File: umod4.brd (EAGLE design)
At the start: 104.9 x 69.8 mm, 101 parts, among them IC1 27C256-FEED-THRU, M1 Generic single-sided NEO-8, M2 RPi Pico W, Q1 DNP/SI2301CDS, Q2 SS8050, U1 RP2040, U2 W25Q128JVSIQ, U3 SY6280AAC, U4 74LVC2G04, U5 74LVC541, U6 74LVC541, U7 74LVC4245, U8 TLV75733P, Y1 12MHz

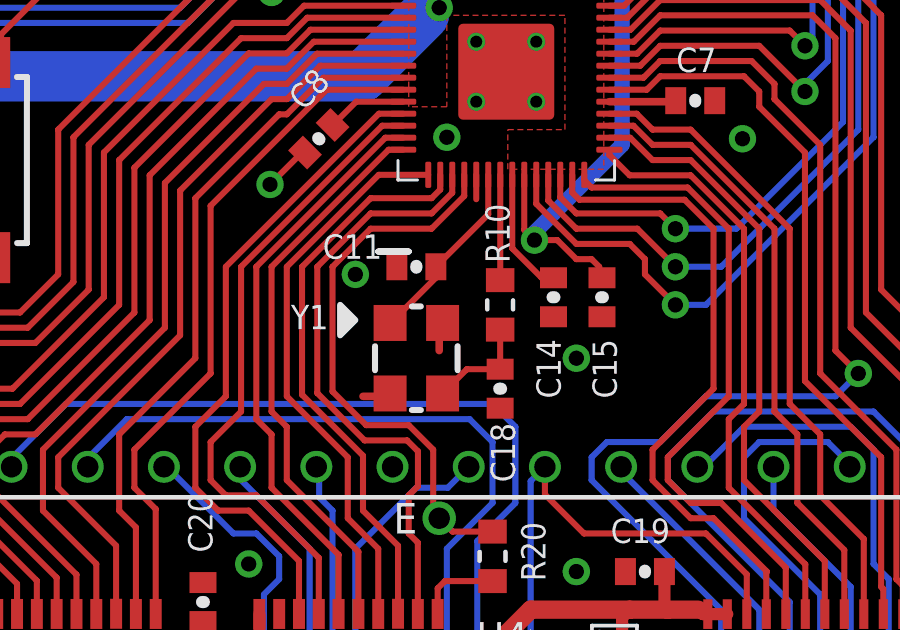
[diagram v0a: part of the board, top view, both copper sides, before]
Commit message: Replace 33pF 0402 packages with SMD-0402-NOM
- Affected parts: C11, C18
- LCSC_PART unchanged
- Manually reworked wire angles on board to clear DRC failures from the new pad geometry
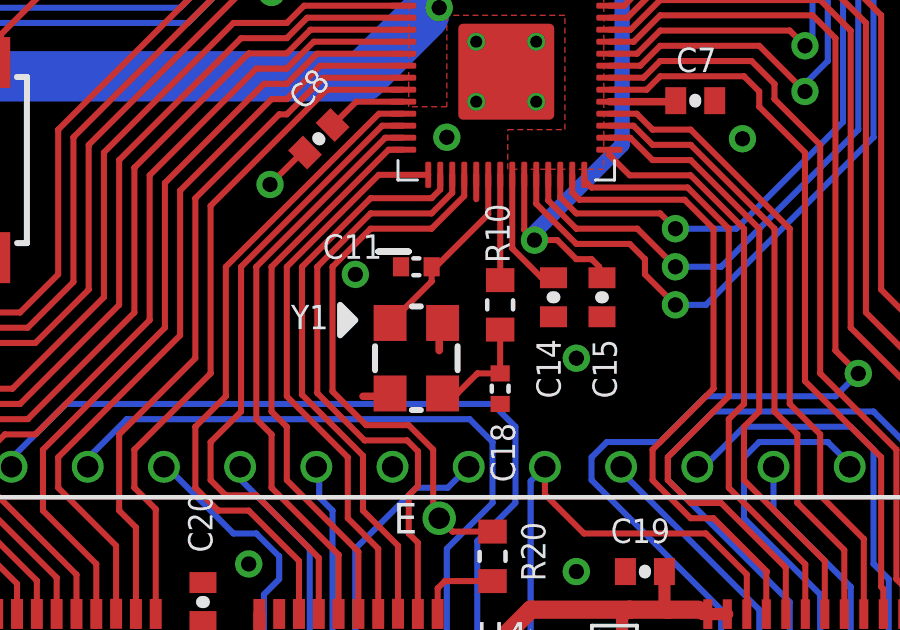
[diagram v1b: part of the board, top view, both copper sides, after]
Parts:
- C11, C18: device SparkFun-03-01-2010:0402-CAP -> robins-v7:SMD-0402-NOM
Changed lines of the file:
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@@
 <attribute name="LCSC_PART" value="C21190" x="87.884" y="35.56" size="1.778" layer="27" rot="R270" display="off"/>
 </element>
-<element name="C11" library="SparkFun-03-01-2010" package="0402-CAP" value="33p/6.3V/COG" x="85.09" y="36.83" smashed="yes">
+<element name="C11" library="robins-v7" package="SMD-0402-NOM" value="33p/6.3V/COG" x="85.09" y="36.83" smashed="yes">
 <attribute name="NAME" x="83.947" y="37.9095" size="0.8128" layer="25" font="vector" ratio="14" rot="R180"/>
 <attribute name="VALUE" x="84.0105" y="35.687" size="0.4064" layer="27"/>
 <attribute name="LCSC_PART" value="C1562" x="85.09" y="36.83" size="1.778" layer="27" display="off"/>
 </element>
-<element name="C18" library="SparkFun-03-01-2010" package="0402-CAP" value="33p/6.3V/COG" x="87.884" y="32.766" smashed="yes" rot="R90">
+<element name="C18" library="robins-v7" package="SMD-0402-NOM" value="33p/6.3V/COG" x="87.884" y="32.766" smashed="yes" rot="R90">
 <attribute name="NAME" x="87.5665" y="31.623" size="0.8128" layer="25" font="vector" ratio="14" rot="R270"/>
 <attribute name="VALUE" x="89.027" y="31.6865" size="0.4064" layer="27" rot="R90"/>
@@
 <contactref element="R10" pad="2"/>
 <contactref element="C18" pad="2"/>
-<wire x1="87.884" y1="33.416" x2="87.884" y2="34.735" width="0.2032" layer="1"/>
-<wire x1="87.884" y1="33.416" x2="86.774" y2="33.416" width="0.2032" layer="1"/>
-<wire x1="86.774" y1="33.416" x2="85.965" y2="32.607" width="0.2032" layer="1"/>
+<wire x1="87.884" y1="33.276" x2="87.884" y2="34.735" width="0.2032" layer="1"/>
+<wire x1="87.884" y1="33.276" x2="87.124" y2="33.276" width="0.2032" layer="1"/>
+<wire x1="85.965" y1="32.607" x2="86.455" y2="32.607" width="0.2032" layer="1"/>
+<wire x1="86.455" y1="32.607" x2="87.124" y2="33.276" width="0.2032" layer="1"/>
 </signal>
 <signal name="N$2">
@@
 <wire x1="87.4872" y1="39.8949" x2="87.4872" y2="38.5772" width="0.2032" layer="1"/>
 <wire x1="84.215" y1="34.957" x2="84.233" y2="34.957" width="0.2032" layer="1"/>
-<wire x1="84.233" y1="34.957" x2="85.74" y2="36.464" width="0.2032" layer="1"/>
-<wire x1="85.74" y1="36.83" x2="85.74" y2="36.464" width="0.2032" layer="1"/>
-<wire x1="87.4872" y1="38.5772" x2="85.74" y2="36.83" width="0.2032" layer="1"/>
+<wire x1="85.6" y1="36.83" x2="85.6" y2="36.342" width="0.2032" layer="1"/>
+<wire x1="85.6" y1="36.342" x2="84.215" y2="34.957" width="0.2032" layer="1"/>
+<wire x1="85.6" y1="36.83" x2="85.74" y2="36.83" width="0.2032" layer="1"/>
+<wire x1="85.74" y1="36.83" x2="87.4872" y2="38.5772" width="0.2032" layer="1"/>
 </signal>
 <signal name="N$5">

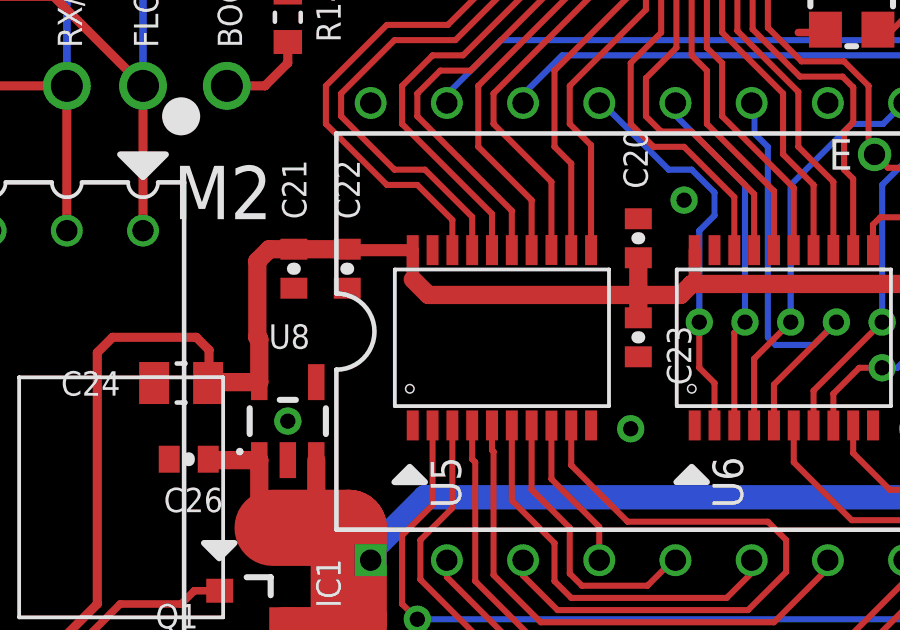
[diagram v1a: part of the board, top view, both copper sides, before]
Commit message: Replace 1uF 0402 packages with SMD-0402-NOM
- Affected parts: C21, C23
- LCSC_PART unchanged
- Manually reworked wire angles on board to clear DRC failures from the new pad geometry
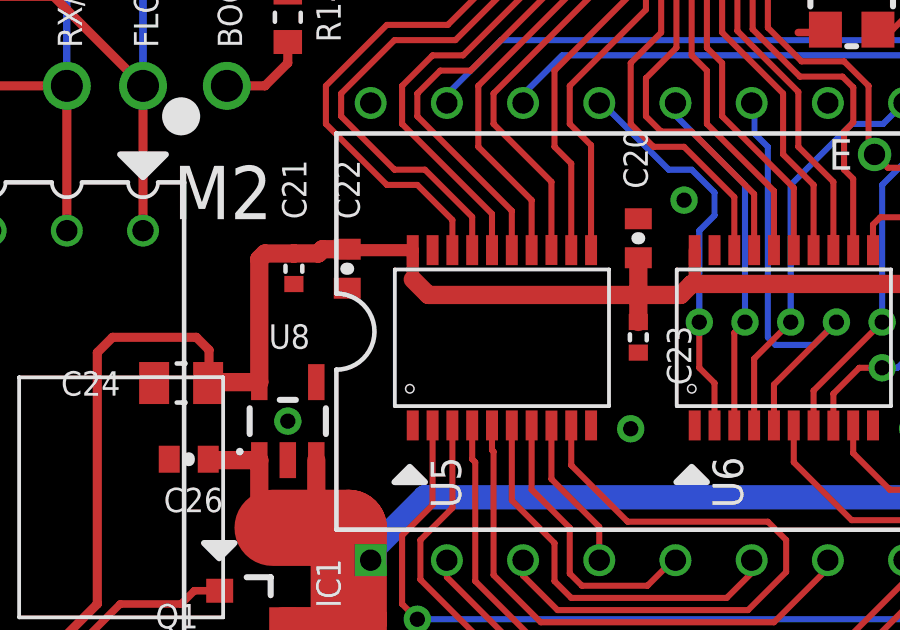
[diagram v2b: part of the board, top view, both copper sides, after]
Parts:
- C21, C23: device SparkFun-03-01-2010:0402-CAP -> robins-v7:SMD-0402-NOM
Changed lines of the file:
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@@
 <attribute name="LCSC_PART" value="C1525" x="77.978" y="25.654" size="1.778" layer="27" rot="R90" display="off"/>
 </element>
-<element name="C23" library="SparkFun-03-01-2010" package="0402-CAP" value="1u/25V/X5R" x="77.978" y="22.352" smashed="yes" rot="R270">
+<element name="C23" library="robins-v7" package="SMD-0402-NOM" value="1u/25V/X5R" x="77.978" y="22.352" smashed="yes" rot="R270">
 <attribute name="NAME" x="78.9305" y="22.733" size="0.8128" layer="25" font="vector" ratio="14" rot="R270"/>
 <attribute name="VALUE" x="76.835" y="23.4315" size="0.4064" layer="27" rot="R270"/>
@@
 <attribute name="LCSC_PART" value="C1525" x="68.2752" y="24.638" size="1.778" layer="27" rot="R270" display="off"/>
 </element>
-<element name="C21" library="SparkFun-03-01-2010" package="0402-CAP" value="1u/25V/X5R" x="66.4972" y="24.638" smashed="yes" rot="R270">
+<element name="C21" library="robins-v7" package="SMD-0402-NOM" value="1u/25V/X5R" x="66.4972" y="24.638" smashed="yes" rot="R270">
 <attribute name="NAME" x="66.9163" y="26.289" size="0.8128" layer="25" font="vector" ratio="14" rot="R90"/>
 <attribute name="VALUE" x="65.3542" y="25.7175" size="0.4064" layer="27" rot="R270"/>
@@
 <wire x1="70.4592" y1="25.257" x2="68.3062" y2="25.257" width="0.4064" layer="1"/>
 <wire x1="68.3062" y1="25.257" x2="68.2752" y2="25.288" width="0.6096" layer="1"/>
-<wire x1="68.2752" y1="25.288" x2="66.4972" y2="25.288" width="0.6096" layer="1"/>
-<wire x1="65.344" y1="20.8581" x2="65.344" y2="22.286" width="0.6096" layer="1"/>
-<wire x1="65.344" y1="22.286" x2="65.278" y2="22.352" width="0.6096" layer="1"/>
-<wire x1="65.278" y1="22.352" x2="65.278" y2="24.892" width="0.6096" layer="1"/>
-<wire x1="65.278" y1="24.892" x2="65.674" y2="25.288" width="0.6096" layer="1"/>
-<wire x1="66.4972" y1="25.288" x2="65.674" y2="25.288" width="0.6096" layer="1"/>
 <wire x1="87.63" y1="24.13" x2="88.9" y2="25.4" width="0.6096" layer="1"/>
 <wire x1="88.9" y1="25.4" x2="92.202" y2="25.4" width="0.6096" layer="1"/>
@@
 <wire x1="77.978" y1="23.764" x2="79.39" y2="23.764" width="0.6096" layer="1"/>
 <wire x1="79.39" y1="23.764" x2="79.756" y2="24.13" width="0.6096" layer="1"/>
-<wire x1="77.978" y1="23.002" x2="77.978" y2="23.764" width="0.6096" layer="1"/>
+<wire x1="77.978" y1="22.862" x2="77.978" y2="23.764" width="0.6096" layer="1"/>
 <wire x1="77.978" y1="25.004" x2="77.978" y2="23.764" width="0.6096" layer="1"/>
 <contactref element="R27" pad="1"/>
@@
 <wire x1="76.962" y1="2.794" x2="76.962" y2="2.286" width="0.3048" layer="1"/>
 <wire x1="76.962" y1="2.286" x2="76.708" y2="2.032" width="0.3048" layer="1"/>
+<wire x1="65.344" y1="20.8581" x2="65.344" y2="24.958" width="0.6096" layer="1"/>
+<wire x1="65.344" y1="24.958" x2="65.532" y2="25.146" width="0.6096" layer="1"/>
+<wire x1="65.532" y1="25.146" x2="66.4952" y2="25.146" width="0.6096" layer="1"/>
+<wire x1="66.4952" y1="25.146" x2="66.4972" y2="25.148" width="0.6096" layer="1"/>
+<wire x1="66.4972" y1="25.148" x2="67.308" y2="25.148" width="0.6096" layer="1"/>
+<wire x1="67.308" y1="25.148" x2="67.31" y2="25.146" width="0.6096" layer="1"/>
+<wire x1="68.2752" y1="25.288" x2="67.448" y2="25.288" width="0.6096" layer="1"/>
+<wire x1="67.448" y1="25.288" x2="67.308" y2="25.148" width="0.6096" layer="1"/>
 </signal>
 <signal name="N$3">

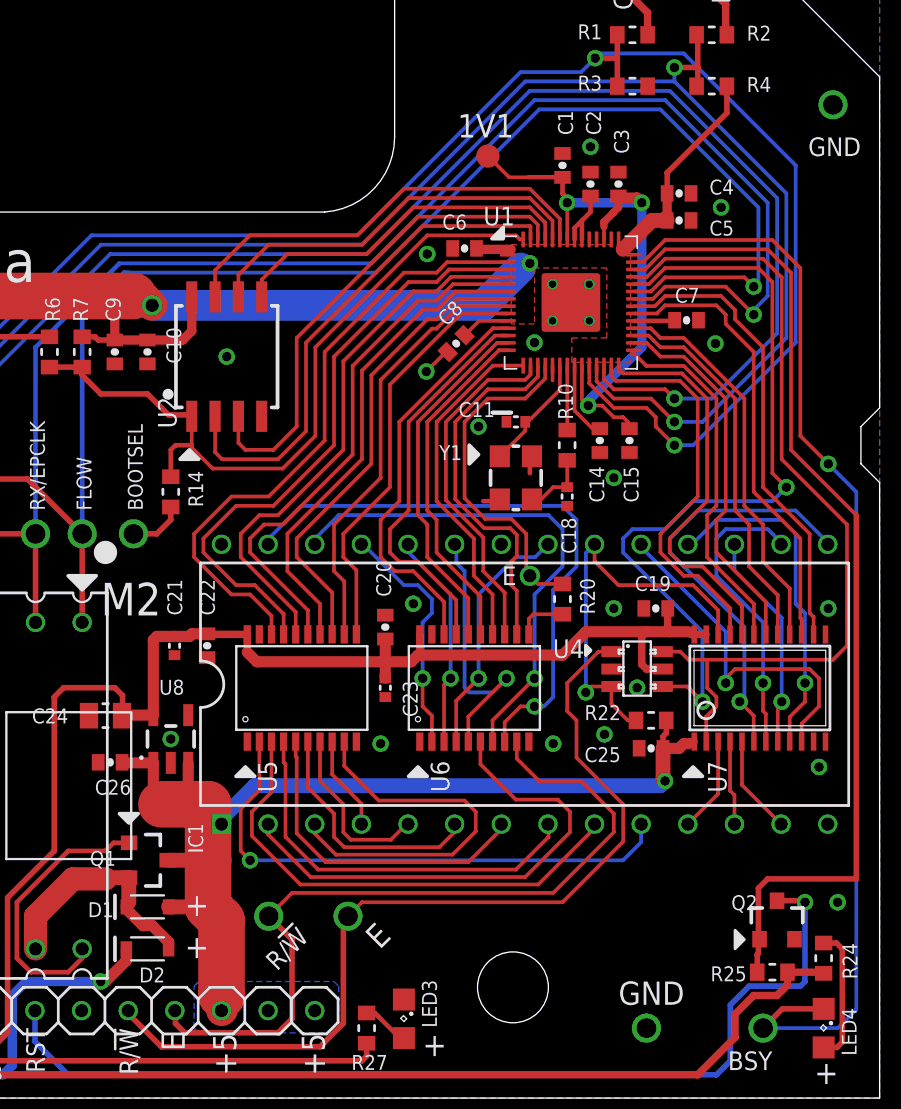
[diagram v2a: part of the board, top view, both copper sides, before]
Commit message: Replace 2.2uF 0402 packages with SMD-0402-NOM
- Affected parts: C3, C4, C10
- LCSC_PART unchanged
- Manually reworked wire angles on board to clear DRC failures from the new pad geometry
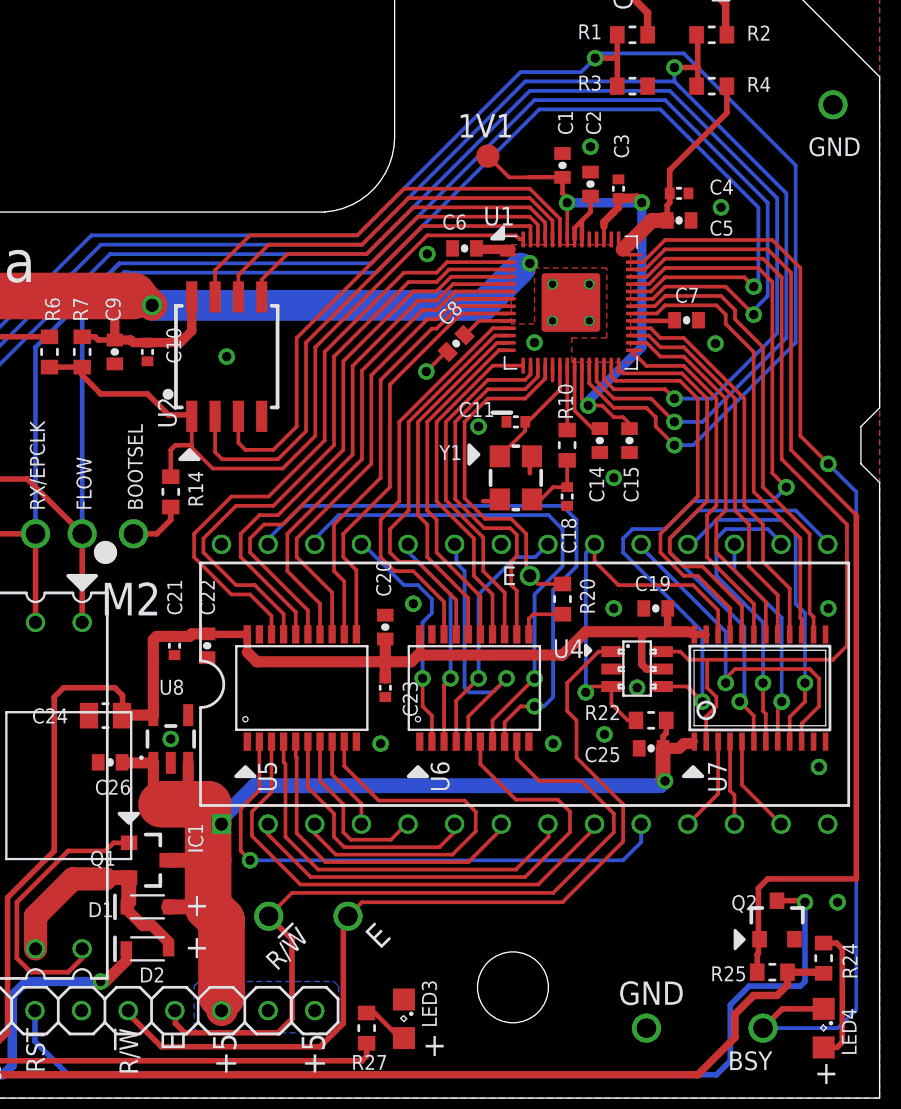
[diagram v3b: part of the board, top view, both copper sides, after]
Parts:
- C10, C3, C4: device SparkFun-03-01-2010:0402-CAP -> robins-v7:SMD-0402-NOM
- moved C3 0.25 mm to (90.7, 49.5)
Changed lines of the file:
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@@
 <attribute name="LCSC_PART" value="C1525" x="63.246" y="40.64" size="1.778" layer="27" rot="R270" display="off"/>
 </element>
-<element name="C10" library="SparkFun-03-01-2010" package="0402-CAP" value="2u2/6.3V/X5R" x="65.024" y="40.64" smashed="yes" rot="R270">
+<element name="C10" library="robins-v7" package="SMD-0402-NOM" value="2u2/6.3V/X5R" x="65.024" y="40.64" smashed="yes" rot="R270">
 <attribute name="NAME" x="66.8655" y="40.005" size="0.8128" layer="25" ratio="14" rot="R90"/>
 <attribute name="VALUE" x="63.881" y="41.7195" size="0.4064" layer="27" rot="R270"/>
 <attribute name="LCSC_PART" value="C12530" x="65.024" y="40.64" size="1.778" layer="27" rot="R270" display="off"/>
 </element>
-<element name="C3" library="SparkFun-03-01-2010" package="0402-CAP" value="2u2/6.3V/X5R" x="90.678" y="49.784" smashed="yes" rot="R90">
-<attribute name="NAME" x="91.2495" y="51.435" size="0.8128" layer="25" font="vector" ratio="14" rot="R90"/>
-<attribute name="VALUE" x="91.821" y="48.7045" size="0.4064" layer="27" rot="R90"/>
-<attribute name="LCSC_PART" value="C12530" x="90.678" y="49.784" size="1.778" layer="27" rot="R90" display="off"/>
-</element>
-<element name="C4" library="SparkFun-03-01-2010" package="0402-CAP" value="2u2/6.3V/X5R" x="93.98" y="49.276" smashed="yes">
+<element name="C3" library="robins-v7" package="SMD-0402-NOM" value="2u2/6.3V/X5R" x="90.678" y="49.53" smashed="yes" rot="R90">
+<attribute name="NAME" x="91.2495" y="51.181" size="0.8128" layer="25" font="vector" ratio="14" rot="R90"/>
+<attribute name="VALUE" x="91.821" y="48.4505" size="0.4064" layer="27" rot="R90"/>
+<attribute name="LCSC_PART" value="C12530" x="90.678" y="49.53" size="1.778" layer="27" rot="R90" display="off"/>
+</element>
+<element name="C4" library="robins-v7" package="SMD-0402-NOM" value="2u2/6.3V/X5R" x="93.98" y="49.276" smashed="yes">
 <attribute name="NAME" x="95.631" y="49.2125" size="0.8128" layer="25" ratio="14"/>
 <attribute name="VALUE" x="92.9005" y="48.133" size="0.4064" layer="27"/>
@@
 <wire x1="83.312" y1="43.18" x2="85.344" y2="45.212" width="1.6764" layer="16"/>
 <via x="85.852" y="45.466" extent="1-16" drill="0.508" diameter="0.3048"/>
-<wire x1="63.246" y1="41.29" x2="65.024" y2="41.29" width="0.508" layer="1"/>
 <wire x1="91.5247" y1="42.3324" x2="93.7016" y2="42.3324" width="0.254" layer="1"/>
 <wire x1="93.7016" y1="42.3324" x2="93.7364" y2="42.3672" width="0.254" layer="1"/>
@@
 <wire x1="63.246" y1="41.29" x2="63.246" y2="43.688" width="0.508" layer="1"/>
 <wire x1="63.246" y1="43.688" x2="64.262" y2="43.688" width="0.8128" layer="1"/>
-<wire x1="65.024" y1="41.29" x2="66.944" y2="41.29" width="0.508" layer="1"/>
-<wire x1="66.944" y1="41.29" x2="67.437" y2="41.783" width="0.508" layer="1"/>
+<wire x1="66.804" y1="41.15" x2="67.437" y2="41.783" width="0.508" layer="1"/>
 <wire x1="88.2872" y1="37.4428" x2="89.266" y2="36.464" width="0.2032" layer="1"/>
 <contactref element="R7" pad="2"/>
-<wire x1="93.33" y1="49.276" x2="93.33" y2="47.8028" width="0.508" layer="1"/>
 <wire x1="93.33" y1="47.8028" x2="92.5068" y2="47.8028" width="0.8128" layer="1"/>
 <wire x1="92.5068" y1="47.8028" x2="90.932" y2="46.228" width="0.8128" layer="1"/>
@@
 <contactref element="R23" pad="1"/>
 <contactref element="R4" pad="1"/>
-<wire x1="93.33" y1="49.276" x2="93.33" y2="50.404" width="0.3048" layer="1"/>
-<wire x1="93.33" y1="50.404" x2="96.583" y2="53.657" width="0.3048" layer="1"/>
+<wire x1="93.47" y1="50.544" x2="96.583" y2="53.657" width="0.3048" layer="1"/>
 <wire x1="41.402" y1="35.56" x2="38.608" y2="35.56" width="1.4224" layer="1"/>
 <contactref element="U3" pad="5"/>
@@
 <wire x1="97.028" y1="4.572" x2="98.044" y2="5.588" width="0.4064" layer="1"/>
 <wire x1="98.044" y1="5.588" x2="99.314" y2="5.588" width="0.4064" layer="1"/>
-<wire x1="99.314" y1="5.588" x2="99.568" y2="5.842" width="0.4064" layer="1"/>
-<wire x1="99.568" y1="5.842" x2="99.71" y2="5.984" width="0.4064" layer="1"/>
 <wire x1="99.885" y1="6.858" x2="101.742" y2="6.858" width="0.4064" layer="1"/>
 <wire x1="3.556" y1="14.732" x2="2.032" y2="14.732" width="0.3048" layer="1"/>
@@
 <wire x1="50.991" y1="30.543" x2="51.308" y2="30.226" width="0.3048" layer="1"/>
 <wire x1="99.885" y1="6.858" x2="99.885" y2="6.159" width="0.4064" layer="1"/>
-<wire x1="99.885" y1="6.159" x2="99.71" y2="5.984" width="0.4064" layer="1"/>
+<wire x1="99.885" y1="6.159" x2="99.314" y2="5.588" width="0.4064" layer="1"/>
+<wire x1="93.47" y1="49.276" x2="93.47" y2="50.544" width="0.3048" layer="1"/>
+<wire x1="93.33" y1="47.8028" x2="93.33" y2="48.626" width="0.3048" layer="1"/>
+<wire x1="93.33" y1="48.626" x2="93.472" y2="48.768" width="0.3048" layer="1"/>
+<wire x1="93.472" y1="48.768" x2="93.472" y2="49.274" width="0.3048" layer="1"/>
+<wire x1="93.472" y1="49.274" x2="93.47" y2="49.276" width="0.3048" layer="1"/>
+<wire x1="65.024" y1="41.15" x2="66.804" y2="41.15" width="0.508" layer="1"/>
+<wire x1="63.246" y1="41.29" x2="64.12" y2="41.29" width="0.508" layer="1"/>
+<wire x1="64.12" y1="41.29" x2="64.262" y2="41.148" width="0.508" layer="1"/>
+<wire x1="64.262" y1="41.148" x2="65.022" y2="41.148" width="0.508" layer="1"/>
+<wire x1="65.022" y1="41.148" x2="65.024" y2="41.15" width="0.508" layer="1"/>
 </signal>
 <signal name="R/!W!_5V">
@@
 <wire x1="87.63" y1="50.15" x2="84.724" y2="50.15" width="0.2032" layer="1"/>
 <wire x1="84.724" y1="50.15" x2="83.566" y2="51.308" width="0.2032" layer="1"/>
-<wire x1="91.948" y1="48.768" x2="91.694" y2="49.022" width="0.6096" layer="1"/>
-<wire x1="91.694" y1="49.022" x2="90.566" y2="49.022" width="0.6096" layer="1"/>
-<wire x1="90.566" y1="49.022" x2="90.678" y2="49.134" width="0.6096" layer="1"/>
 <wire x1="89.8872" y1="47.4692" x2="89.8872" y2="47.71700625" width="0.4064" layer="1"/>
 <wire x1="89.8872" y1="47.71700625" x2="90.39921875" y2="48.229025" width="0.4064" layer="1"/>
 <wire x1="90.39921875" y1="48.229025" x2="90.39921875" y2="48.23521875" width="0.3048" layer="1"/>
 <wire x1="90.39921875" y1="48.23521875" x2="90.678" y2="48.514" width="0.4064" layer="1"/>
-<wire x1="90.678" y1="48.514" x2="90.678" y2="49.134" width="0.4064" layer="1"/>
+<wire x1="90.678" y1="48.514" x2="90.678" y2="49.02" width="0.4064" layer="1"/>
 <wire x1="87.884" y1="48.768" x2="87.884" y2="49.022" width="0.254" layer="1"/>
 <wire x1="87.884" y1="49.022" x2="87.63" y2="49.276" width="0.254" layer="1"/>
@@
 <wire x1="87.884" y1="48.768" x2="87.884" y2="48.514" width="0.2032" layer="1"/>
 <wire x1="87.884" y1="48.514" x2="87.8872" y2="48.5108" width="0.2032" layer="1"/>
+<wire x1="90.678" y1="49.02" x2="91.696" y2="49.02" width="0.508" layer="1"/>
+<wire x1="91.696" y1="49.02" x2="91.948" y2="48.768" width="0.508" layer="1"/>
 </signal>
 <signal name="N$32">
